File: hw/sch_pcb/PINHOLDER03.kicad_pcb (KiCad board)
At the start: 2 copper layers, 50.3 x 30 mm, 9 parts, among them J1 HEADER_1x03, J2 HEADER_1x02, M1 HOLE, M2 HOLE, M3 HOLE, M4 HOLE

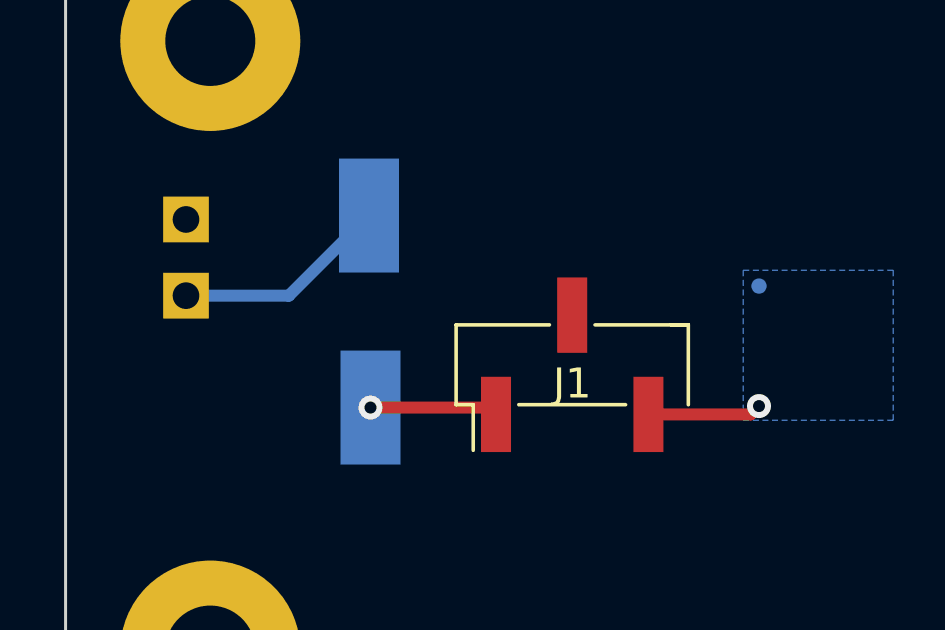
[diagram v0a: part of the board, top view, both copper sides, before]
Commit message: Fix typo in the name. Cleanup layout.
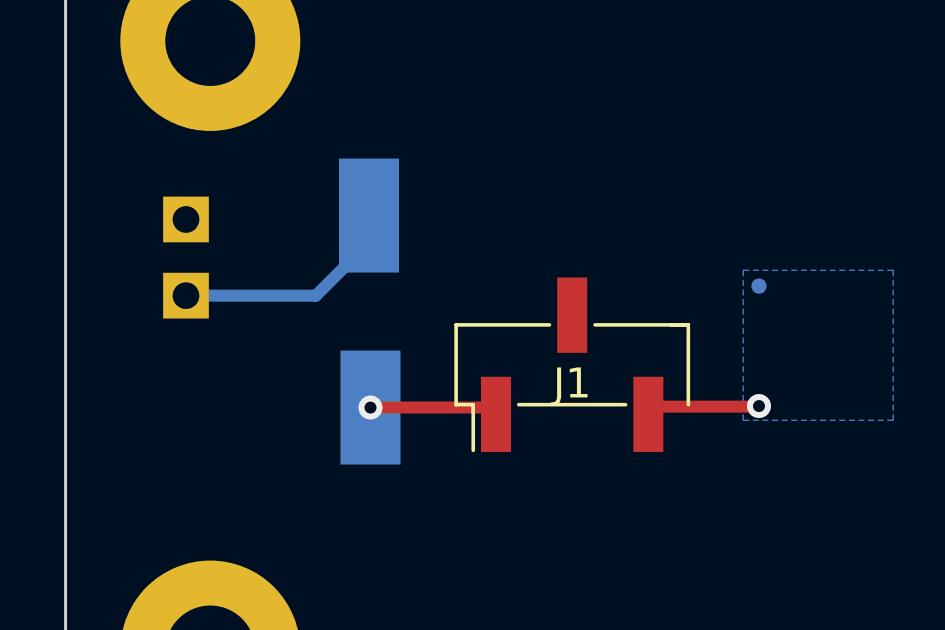
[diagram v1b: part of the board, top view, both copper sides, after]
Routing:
- net Net-(D1-Pad2): track 7.21 -> 7.73 mm
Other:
- board text added: "PINHOLDER03A"
- board text removed: "PINHOLDER02A"
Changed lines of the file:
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@@
     (effects (font (size 1.5 1.5) (thickness 0.3)) (justify mirror))
   )
-  (gr_text "PINHOLDER02A" (at 175.75 74.95) (layer "B.SilkS")
+  (gr_text "PINHOLDER03A" (at 175.75 74.95) (layer "B.SilkS")
     (effects (font (size 1.7 1.7) (thickness 0.3)) (justify mirror))
   )
@@
     (effects (font (size 1.5 1.5) (thickness 0.3)) (justify mirror))
   )
-  (segment (start 164.214 88.929) (end 167.621 88.929) (width 0.4) (layer "F.Cu") (net 1))
-  (segment (start 167.621 88.929) (end 167.9 88.65) (width 0.4) (layer "F.Cu") (net 1))
+  (segment (start 167.8786 88.6714) (end 167.9 88.65) (width 0.4) (layer "F.Cu") (net 1))
+  (segment (start 164.4716 88.6714) (end 167.8786 88.6714) (width 0.4) (layer "F.Cu") (net 1))
+  (segment (start 164.214 88.929) (end 164.4716 88.6714) (width 0.4) (layer "F.Cu") (net 1))
   (via (at 167.9 88.65) (size 0.8) (drill 0.4) (layers "F.Cu" "B.Cu") (net 1))
   (segment (start 158.905 88.7) (end 159.134 88.929) (width 0.4) (layer "F.Cu") (net 3))
   (segment (start 154.95 88.7) (end 158.905 88.7) (width 0.4) (layer "F.Cu") (net 3))
   (via (at 154.95 88.7) (size 0.8) (drill 0.4) (layers "F.Cu" "B.Cu") (net 3))
-  (segment (start 154.9 82.3) (end 152.23 84.97) (width 0.4) (layer "B.Cu") (net 4))
-  (segment (start 152.23 84.97) (end 148.8 84.97) (width 0.4) (layer "B.Cu") (net 4))
+  (segment (start 154.9 83.1996) (end 153.1296 84.97) (width 0.4) (layer "B.Cu") (net 4))
+  (segment (start 154.9 82.3) (end 154.9 83.1996) (width 0.4) (layer "B.Cu") (net 4))
+  (segment (start 153.1296 84.97) (end 148.8 84.97) (width 0.4) (layer "B.Cu") (net 4))
   (zone (net 2) (net_name "GND") (layer "F.Cu") (hatch edge 0.508)
     (connect_pads (clearance 0.4))

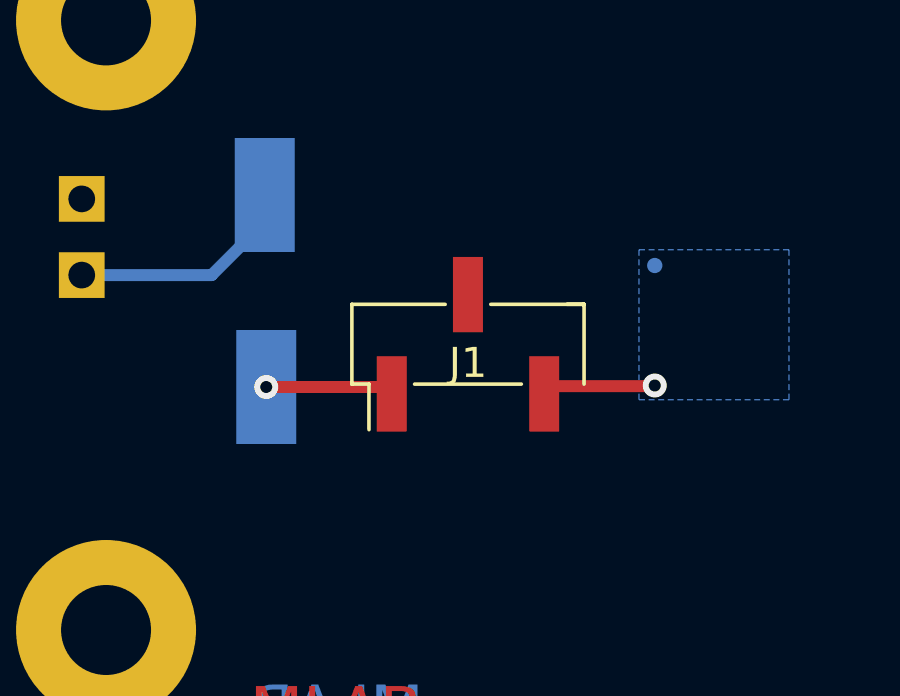
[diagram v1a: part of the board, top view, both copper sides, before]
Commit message: zamena anoda-katoda diody
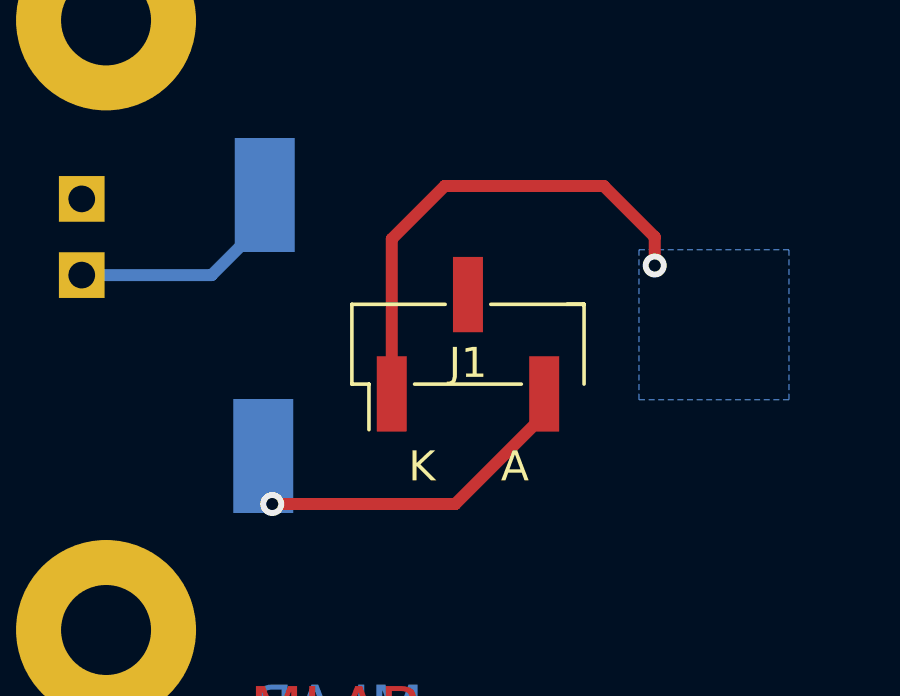
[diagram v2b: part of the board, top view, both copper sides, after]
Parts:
- moved TP2 2.30 mm to (154.8, 91.0)
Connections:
- J1 pad 1: Net-(J1-Pad1) -> /circle_0
- J1 pad 3: /circle_0 -> Net-(D2-Pad2)
- TP2 pad 1: Net-(J1-Pad1) -> Net-(D2-Pad2)
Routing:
- net /circle_0: track 3.80 -> 16.6 mm
- net Net-(D2-Pad2): track 0.00 -> 11.4 mm, vias 0 -> 1
- net Net-(J1-Pad1): track 4.28 -> 0.00 mm, vias 1 -> 0
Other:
- board text added: "A"
- board text added: "K A"
- board text removed: "Top"
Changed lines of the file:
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@@
   (net 1 "/circle_0")
   (net 2 "GND")
-  (net 3 "Net-(J1-Pad1)")
+  (net 3 "Net-(D2-Pad2)")
   (net 4 "Net-(D1-Pad2)")
   (footprint "Mlab_Mechanical:MountingHole_3mm" placed (layer "F.Cu")
@@
     (fp_line (start 2.54 0.32) (end 1.27 0.32) (layer "F.Fab") (width 0.1))
     (pad "1" smd rect locked (at -1.655 -2.54 90) (size 2.51 1) (layers "F.Cu" "F.Paste" "F.Mask")
-      (net 3 "Net-(J1-Pad1)") (pintype "input"))
+      (net 1 "/circle_0") (pintype "input"))
     (pad "2" smd rect locked (at 1.655 0 90) (size 2.51 1) (layers "F.Cu" "F.Paste" "F.Mask")
       (net 2 "GND") (pintype "input"))
     (pad "3" smd rect locked (at -1.655 2.54 90) (size 2.51 1) (layers "F.Cu" "F.Paste" "F.Mask")
-      (net 1 "/circle_0") (pintype "input"))
+      (net 3 "Net-(D2-Pad2)") (pintype "input"))
     (model "${KICAD6_3DMODEL_DIR}/Connector_PinHeader_2.54mm.3dshapes/PinHeader_1x03_P2.54mm_Vertical_SMD_Pin1Left.wrl"
       (offset (xyz 0 0 0))
@@
   )
   (footprint "TestPoint:TestPoint_Keystone_5019_Minature" (layer "B.Cu")
-    (at 154.95 88.7 90)
+    (at 154.85 91 90)
     (descr "SMT Test Point- Micro Miniature 5019, http://www.keyelco.com/product-pdf.cfm?p=1357")
     (tags "Test Point")
@@
     (fp_line (start 0 -0.5) (end 0 -1) (layer "B.Fab") (width 0.15))
     (pad "1" smd rect (at 0 0 90) (size 3.8 2) (layers "B.Cu" "B.Paste" "B.Mask")
-      (net 3 "Net-(J1-Pad1)") (pinfunction "1") (pintype "passive"))
+      (net 3 "Net-(D2-Pad2)") (pinfunction "1") (pintype "passive"))
     (model "${KICAD6_3DMODEL_DIR}/TestPoint.3dshapes/TestPoint_Keystone_5019_Minature.wrl"
       (offset (xyz 0 0 0))
@@
     (effects (font (size 1.5 1.5) (thickness 0.3)) (justify mirror))
   )
-  (gr_text "Top" (at 152.1 88.7 -90) (layer "B.SilkS")
+  (gr_text "A" (at 151.95 91.05 -90) (layer "B.SilkS")
     (effects (font (size 1.5 1.5) (thickness 0.3)) (justify mirror))
   )
@@
     (effects (font (size 1.5 1.5) (thickness 0.3)) (justify mirror))
   )
-  (segment (start 167.8786 88.6714) (end 167.9 88.65) (width 0.4) (layer "F.Cu") (net 1))
-  (segment (start 164.4716 88.6714) (end 167.8786 88.6714) (width 0.4) (layer "F.Cu") (net 1))
-  (segment (start 164.214 88.929) (end 164.4716 88.6714) (width 0.4) (layer "F.Cu") (net 1))
-  (via (at 167.9 88.65) (size 0.8) (drill 0.4) (layers "F.Cu" "B.Cu") (net 1))
-  (segment (start 158.905 88.7) (end 159.134 88.929) (width 0.4) (layer "F.Cu") (net 3))
-  (segment (start 154.95 88.7) (end 158.905 88.7) (width 0.4) (layer "F.Cu") (net 3))
-  (via (at 154.95 88.7) (size 0.8) (drill 0.4) (layers "F.Cu" "B.Cu") (net 3))
+  (gr_text "K     A" (at 161.7 91.35) (layer "F.SilkS")
+    (effects (font (size 1 1) (thickness 0.15)))
+  )
+  (segment (start 158.905 88.7) (end 159.134 88.929) (width 0.4) (layer "F.Cu") (net 1))
+  (segment (start 167.9 83.7) (end 167.9 84.65) (width 0.4) (layer "F.Cu") (net 1))
+  (segment (start 159.134 83.766) (end 160.9 82) (width 0.4) (layer "F.Cu") (net 1))
+  (segment (start 159.134 88.929) (end 159.134 83.766) (width 0.4) (layer "F.Cu") (net 1))
+  (segment (start 166.2 82) (end 167.9 83.7) (width 0.4) (layer "F.Cu") (net 1))
+  (segment (start 160.9 82) (end 166.2 82) (width 0.4) (layer "F.Cu") (net 1))
+  (via (at 167.9 84.65) (size 0.8) (drill 0.4) (layers "F.Cu" "B.Cu") (net 1))
+  (segment (start 164.214 88.929) (end 164.214 89.636) (width 0.4) (layer "F.Cu") (net 3))
+  (segment (start 161.25 92.6) (end 155.15 92.6) (width 0.4) (layer "F.Cu") (net 3))
+  (segment (start 164.214 88.929) (end 164.4716 88.6714) (width 0.4) (layer "F.Cu") (net 3))
+  (segment (start 164.214 89.636) (end 161.25 92.6) (width 0.4) (layer "F.Cu") (net 3))
+  (via (at 155.15 92.6) (size 0.8) (drill 0.4) (layers "F.Cu" "B.Cu") (net 3))
   (segment (start 154.9 83.1996) (end 153.1296 84.97) (width 0.4) (layer "B.Cu") (net 4))
   (segment (start 154.9 82.3) (end 154.9 83.1996) (width 0.4) (layer "B.Cu") (net 4))
